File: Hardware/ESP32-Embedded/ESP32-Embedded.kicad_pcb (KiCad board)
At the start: 2 copper layers, 50 x 50 mm, 27 parts, among them J1 Micro USB, Q1 S8050, Q2 S8050, SW1 SW_Push, SW2 SW_Push, U1 ESP32-WROOM-32E, U2 AMS1117-3.3, U3 CH340G, Y1 12Mhz

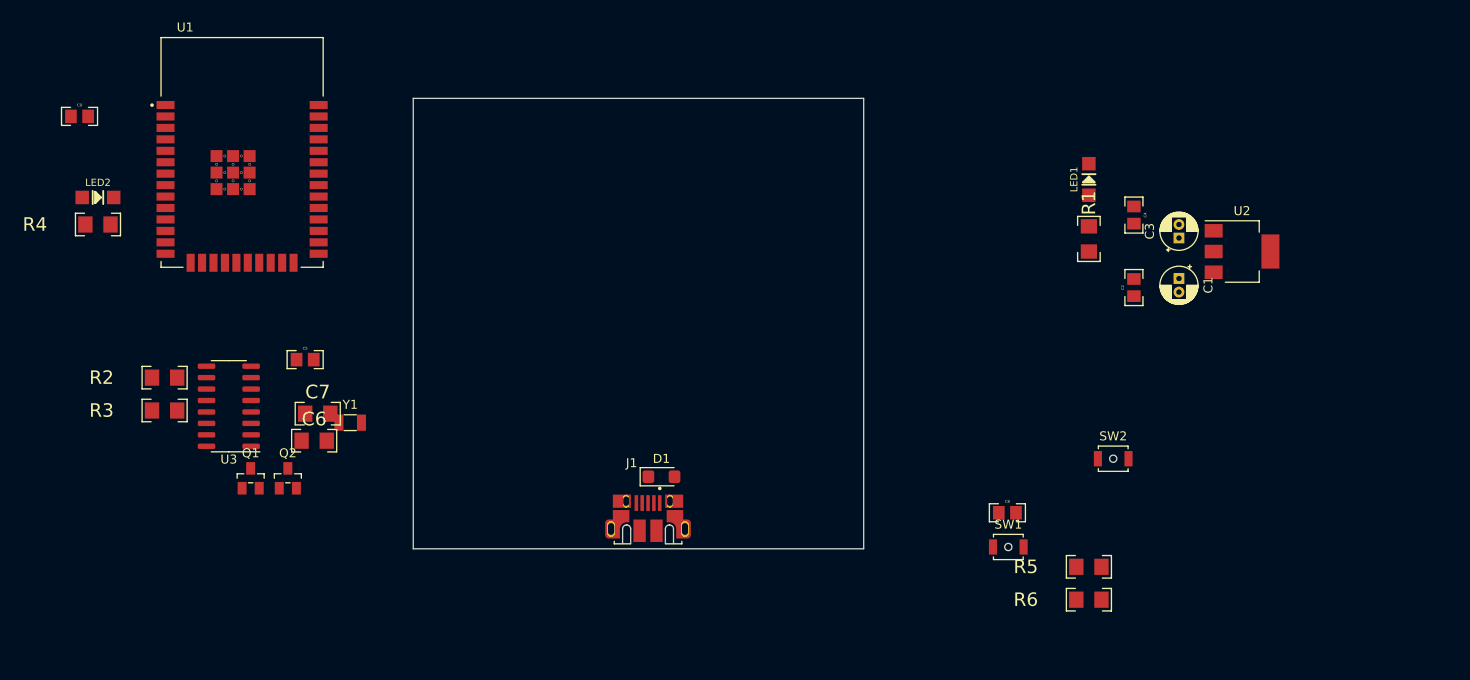
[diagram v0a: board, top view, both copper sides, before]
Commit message: ordenando componentes en placa
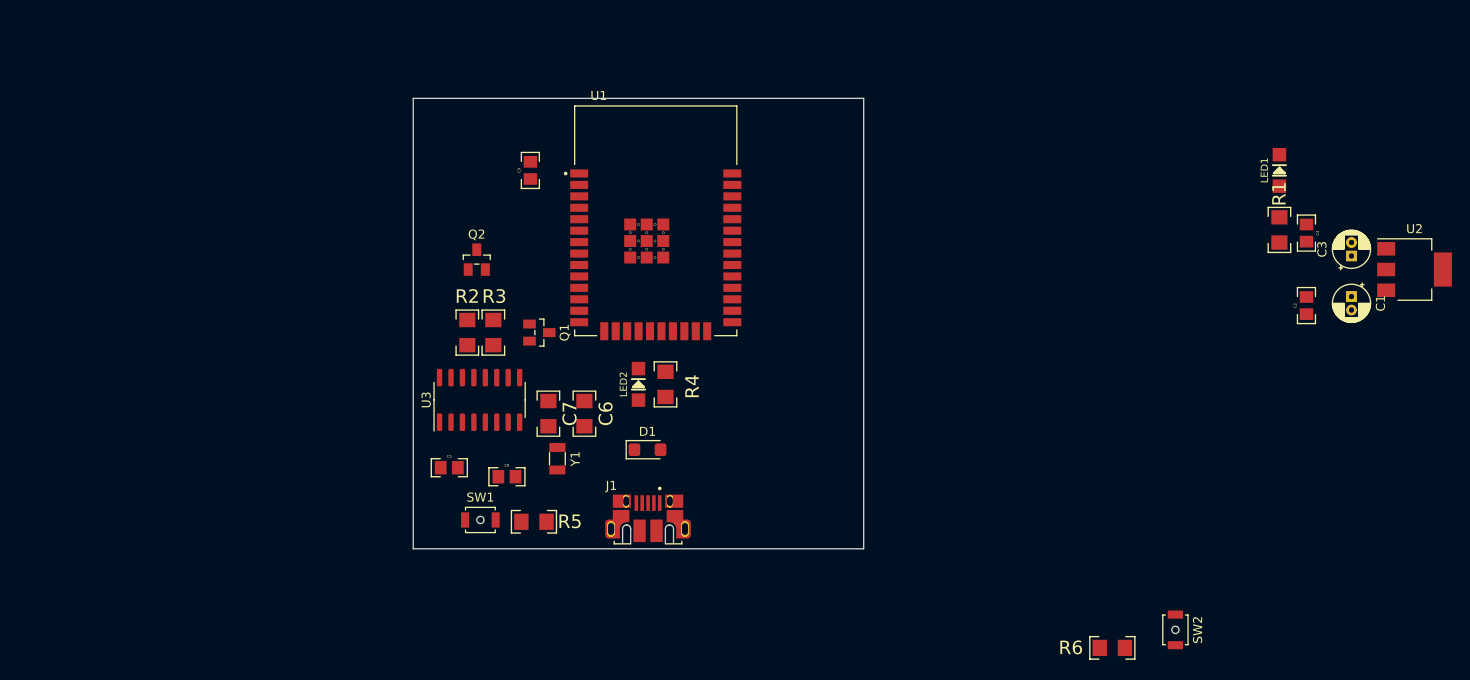
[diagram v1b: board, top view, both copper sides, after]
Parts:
- SW1: value SW_Push -> EN
- SW2: value SW_Push -> BOOT
- moved R4 65.5 mm to (148.0, 111.7), turned to 90 degrees
- moved LED2 63.5 mm to (145.0, 111.7), turned to 90 degrees
- moved R5 61.8 mm to (133.4, 127.0), turned to 180 degrees
- moved SW1 58.7 mm to (127.5, 126.8)
- moved C8 55.7 mm to (130.4, 122.0)
- moved C9 50.4 mm to (133.0, 88.0), turned to 90 degrees
- moved U1 46.5 mm to (146.9, 93.6)
- moved R3 37.5 mm to (128.9, 106.0), turned to -90 degrees
- moved Q1 35.9 mm to (134.0, 106.0), turned to -90 degrees
- moved R2 34.0 mm to (126.0, 106.0), turned to -90 degrees
- moved Q2 32.1 mm to (127.0, 97.9)
- moved C6 30.1 mm to (139.0, 115.0), turned to -90 degrees
- moved U3 27.8 mm to (127.4, 113.5), turned to 90 degrees
- moved C7 25.6 mm to (135.0, 115.0), turned to -90 degrees
- moved Y1 23.3 mm to (136.0, 120.0), turned to -90 degrees
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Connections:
- Q1 pad B: (no net) -> Net-(Q1-PadB)
- Q1 pad C: (no net) -> /IO0
- Q1 pad E: (no net) -> /DTR
- Q2 pad B: (no net) -> Net-(Q2-PadB)
- Q2 pad C: (no net) -> /EN
- Q2 pad E: (no net) -> /RTS
- R2 pad 2: Net-(Q1-B) -> Net-(Q1-PadB)
- R3 pad 2: Net-(Q2-B) -> Net-(Q2-PadB)
- U1 pad 1: (no net) -> GND
- U1 pad 15: unconnected-(U1-IO26-Pad15) -> GND
- U1 pad 19: (no net) -> unconnected-(U1-CMD-Pad19)
- U1 pad 2: (no net) -> +3V3
- U1 pad 22: /IO2 -> unconnected-(U1-SD1-Pad22)
- U1 pad 23: /IO0 -> unconnected-(U1-IO15-Pad23)
- U1 pad 24: unconnected-(U1-IO4-Pad24) -> /IO2
- U1 pad 25: unconnected-(U1-IO16-Pad25) -> /IO0
- U1 pad 26: (no net) -> unconnected-(U1-IO4-Pad26)
- U1 pad 3: (no net) -> /EN
- U1 pad 34: unconnected-(U1-IO5-Pad34) -> /RXD0
- U1 pad 35: unconnected-(U1-IO18-Pad35) -> /TXD0
- U1 pad 37: (no net) -> unconnected-(U1-IO23-Pad37)
- U1 pad 38: unconnected-(U1-IO19-Pad38) -> GND
- U1 pad 4: (no net) -> unconnected-(U1-SENSOR_VP-Pad4)
- U1 pad 6: (no net) -> unconnected-(U1-IO34-Pad6)
- U1 pad 7: (no net) -> unconnected-(U1-IO35-Pad7)
- U1 pad 9: /EN -> unconnected-(U1-IO33-Pad9)

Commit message: placa con esp32 embebido y 5 puentes lista
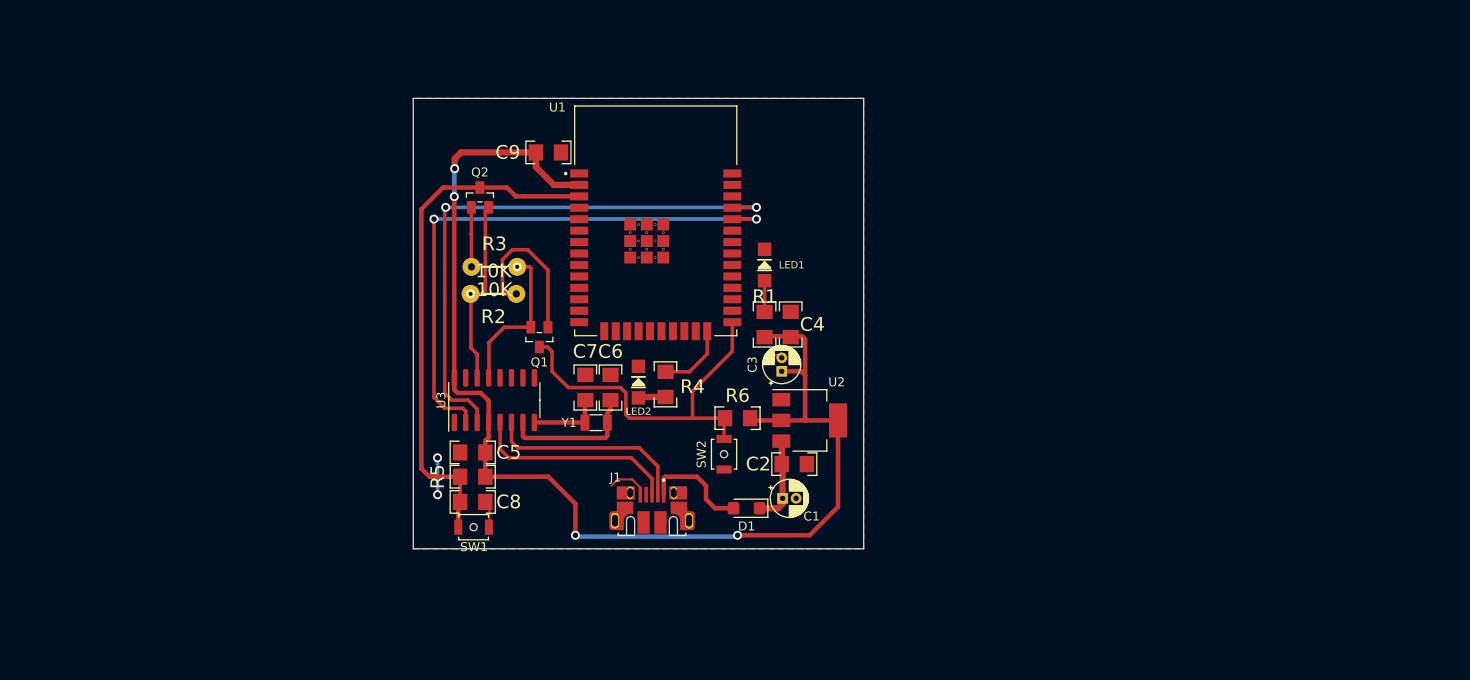
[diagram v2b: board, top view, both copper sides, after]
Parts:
- C2, C4, C5, C8, C9: footprint EESTN5:C_0805 -> EESTN5:C_1206
- R2, R3: footprint EESTN5:R_1206 -> EESTN5:RES0.2
- SW1: value EN -> SW_Push
- SW2: value BOOT -> SW_Push
- moved U2 69.2 mm to (164.0, 115.7)
- moved C1 67.0 mm to (161.0, 124.4), turned to 0 degrees
- moved C3 64.5 mm to (160.9, 110.3)
- moved C2 59.5 mm to (162.3, 120.6), turned to 180 degrees
- moved C4 58.1 mm to (161.9, 105.1)
- moved LED1 58.1 mm to (159.0, 98.5)
- moved R1 58.1 mm to (159.0, 105.1)
- moved SW2 53.8 mm to (154.5, 119.5), turned to 90 degrees
- moved R6 48.8 mm to (156.0, 115.5), turned to 180 degrees
- moved D1 12.8 mm to (157.0, 125.5), turned to 180 degrees
- moved R5 8.44 mm to (126.6, 122.0)
- moved R3 7.30 mm to (129.0, 98.7), turned to 180 degrees
- moved Q2 6.91 mm to (127.4, 91.0)
- moved Y1 5.87 mm to (140.3, 116.0), turned to 0 degrees
- moved R2 5.19 mm to (128.9, 101.7), turned to 0 degrees
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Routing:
- net +3V3: track 0.00 -> 136.4 mm, vias 0 -> 4
- net /RXD0: track 0.00 -> 63.7 mm, vias 0 -> 2
- net /TXD0: track 0.00 -> 63.7 mm, vias 0 -> 2
- net /EN: track 0.00 -> 58.1 mm
- net /IO0: track 0.00 -> 41.4 mm
- net /D+: track 0.00 -> 23.0 mm
- net /D-: track 0.00 -> 22.7 mm
- net /RTS: track 0.00 -> 20.8 mm
- net Net-(Q1-PadB): track 0.00 -> 18.0 mm
- net /DTR: track 0.00 -> 17.4 mm
- net GND: track 0.00 -> 15.4 mm, vias 0 -> 2
- net Net-(U3-XI): track 0.00 -> 15.2 mm
- net Net-(D1-A): track 0.00 -> 12.0 mm
- net +5V: track 0.00 -> 9.77 mm
- net Net-(U3-XO): track 0.00 -> 8.14 mm
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- added copper zone on F.Cu, net GND

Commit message: placa v2 con 3 puentes
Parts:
- moved U1 1.72 mm to (146.7, 95.3)
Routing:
- net /RXD0: track 63.7 -> 88.2 mm, vias 2 -> 0
- net /TXD0: track 63.7 -> 81.8 mm, vias 2 -> 0
- net +3V3: track 136.4 -> 138.6 mm, vias 4 -> 2
- net /IO0: track 41.4 -> 39.6 mm
- net /EN: track 58.1 -> 56.6 mm, vias 0 -> 2
- net /IO2: track 7.98 -> 6.59 mm

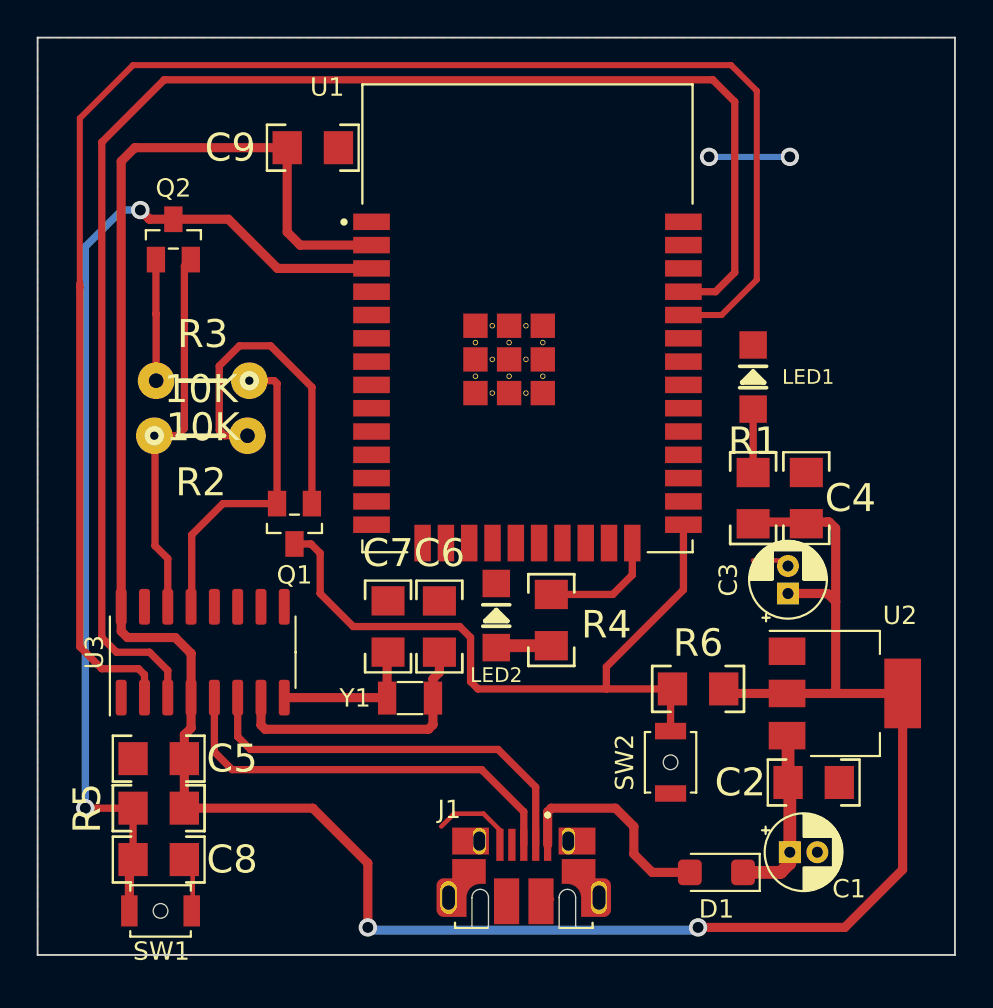
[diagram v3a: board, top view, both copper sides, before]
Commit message: Hice cambios de tamaño de pistas y margen de gnd añadi 3d a componentes y agregue imagenes de los 3D
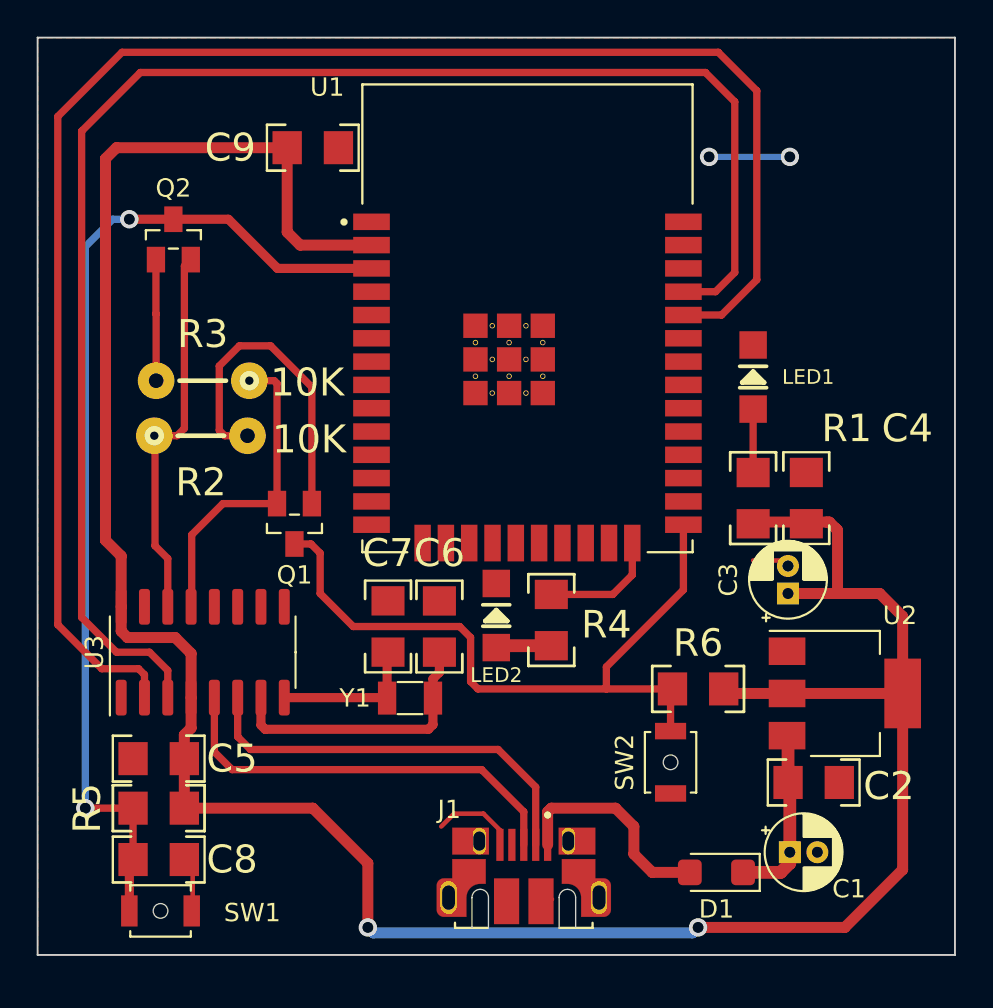
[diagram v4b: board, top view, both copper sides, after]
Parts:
- SW1: value SW_Push -> EN
- SW2: value SW_Push -> BOOT
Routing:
- net +3V3: track 138.6 -> 142.8 mm
- net /TXD0: track 81.8 -> 84.0 mm
- net /RXD0: track 88.2 -> 90.3 mm

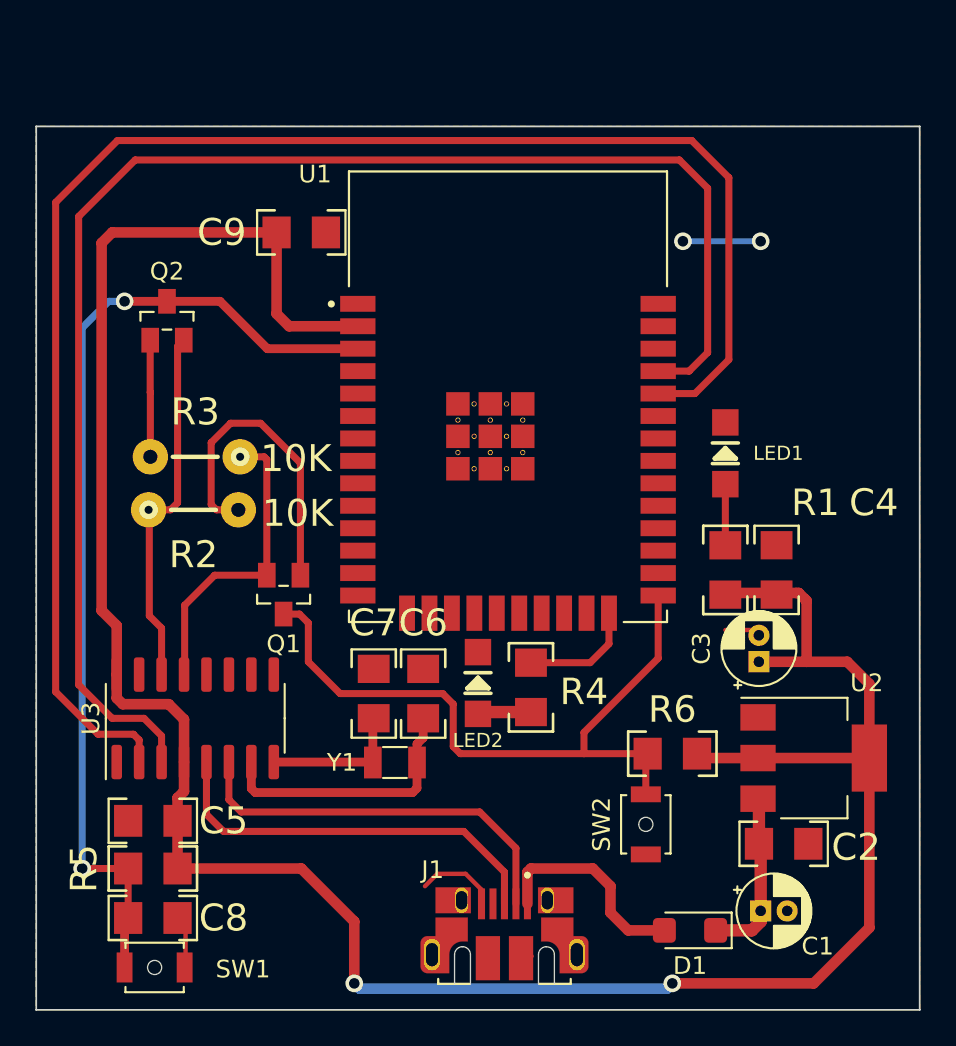
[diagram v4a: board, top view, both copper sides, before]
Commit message: Cambios importantes correcciones con Bustos placa lista
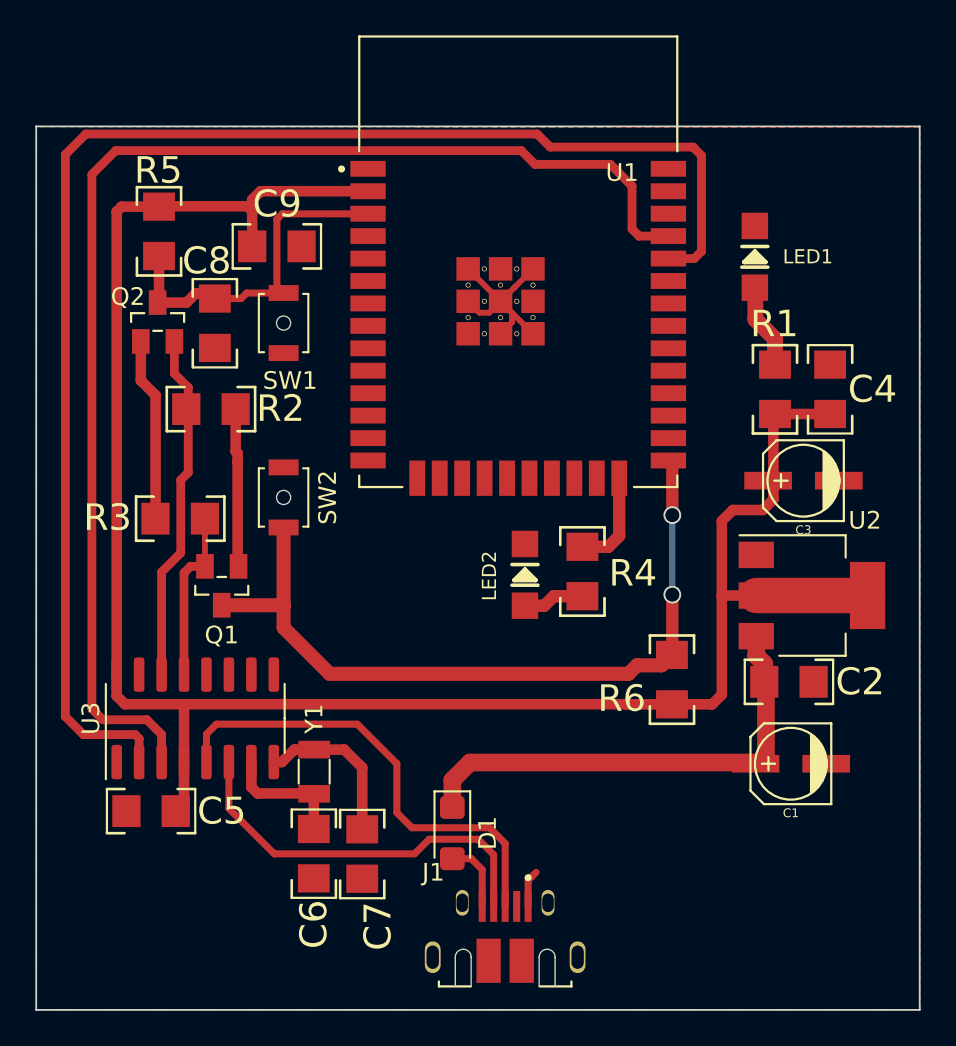
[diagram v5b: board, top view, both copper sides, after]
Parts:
- C1, C3: footprint Capacitor_THT:CP_Radial_D4.0mm_P1.50mm -> EESTN5:CAP_ELEC_SMD_4X5.5
- R2, R3: footprint EESTN5:RES0.2 -> EESTN5:R_1206
- moved SW1 37.2 mm to (134.0, 91.1), turned to 90 degrees
- moved R5 36.1 mm to (127.0, 85.9), turned to -90 degrees
- moved C8 33.8 mm to (130.1, 91.1), turned to 90 degrees
- moved SW2 27.6 mm to (134.0, 101.0), turned to -90 degrees
- moved D1 14.5 mm to (143.6, 120.0), turned to -90 degrees
- moved LED1 11.2 mm to (160.7, 87.4)
- moved C6 11.0 mm to (135.7, 121.2), turned to 90 degrees
- moved C4 10.7 mm to (164.9, 94.9)
- moved R1 10.6 mm to (161.8, 94.9)
- moved C3 10.6 mm to (163.4, 100.0), turned to 180 degrees
- moved U2 9.20 mm to (163.9, 106.5)
- moved C2 9.17 mm to (162.6, 111.4)
- moved C7 9.11 mm to (138.4, 121.2), turned to 90 degrees
- moved C1 8.50 mm to (162.7, 116.1), turned to 180 degrees
- moved U1 7.66 mm to (147.3, 87.7)
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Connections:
- U1 pad 38: GND -> unconnected-(U1-GND-Pad38)
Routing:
- net /EN: track 56.2 -> 19.9 mm, vias 2 -> 0
- net +3V3: track 142.8 -> 115.2 mm, vias 2 -> 0
- net +5V: track 9.77 -> 27.0 mm
- net /TXD0: track 84.0 -> 73.0 mm
- net Net-(Q1-PadB): track 18.0 -> 8.97 mm
- net /RXD0: track 90.3 -> 82.3 mm
- net Net-(U3-XI): track 15.2 -> 7.13 mm
- net Net-(D1-A): track 12.0 -> 4.06 mm
- net /DTR: track 17.4 -> 9.52 mm
- net /IO0: track 39.6 -> 43.8 mm, vias 0 -> 2
- net Net-(Q2-PadB): track 6.60 -> 10.7 mm
- net /D+: track 23.0 -> 26.7 mm
- net Net-(LED1-A): track 3.46 -> 4.83 mm
- net Net-(U3-XO): track 8.14 -> 9.21 mm
- net /RTS: track 20.8 -> 19.8 mm
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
